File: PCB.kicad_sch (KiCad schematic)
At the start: 13 parts, among them J1 Conn_ARM_SWD_TagConnect_TC2030, U2 STM32L476RGTx

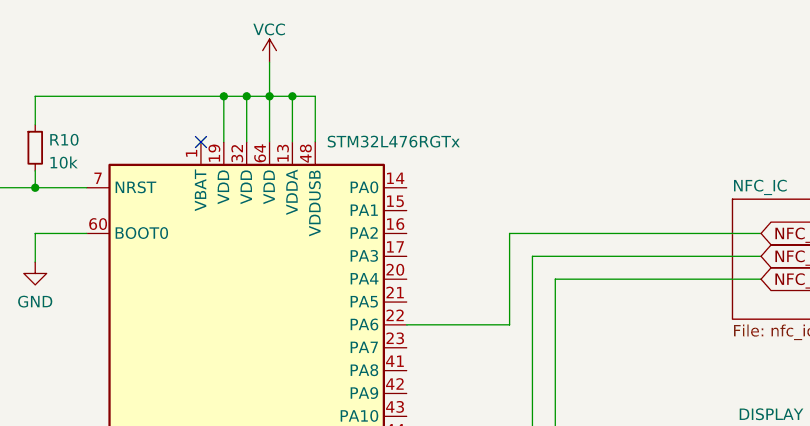
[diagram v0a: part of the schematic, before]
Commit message: Add board REV-D
Revision D changes the mounting holes so that we can fit screws to
assemble the two case pieces.

Also add required compliance logos on the back.
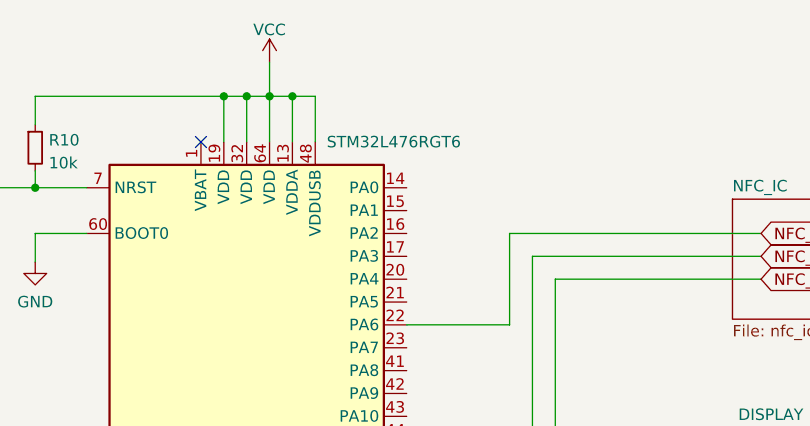
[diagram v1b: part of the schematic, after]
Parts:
- U2: value STM32L476RGTx -> STM32L476RGT6
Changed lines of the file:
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@@
       (effects (font (size 1.27 1.27)) (justify left))
     )
-    (property "Value" "STM32L476RGTx" (at 73.66 32.385 0)
+    (property "Value" "STM32L476RGT6" (at 73.66 32.385 0)
       (effects (font (size 1.27 1.27)) (justify left))
     )
